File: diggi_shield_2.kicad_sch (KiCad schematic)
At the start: 100 parts, among them J1_P1 IN_L, J1_P2 IN_GND, J1_P3 IN_R, J1_P4 OUT_R, J1_P5 OUT_GND, J1_P6 OUT_L, J2_P1 HP_R, J2_P2 HP_GND, J2_P3 HP_L, J8_P1 GND, J8_P2 +5V, J8_P3 MIDI_RX*, J8_P4 MIDI_TX, J8_P5 VBUS_END

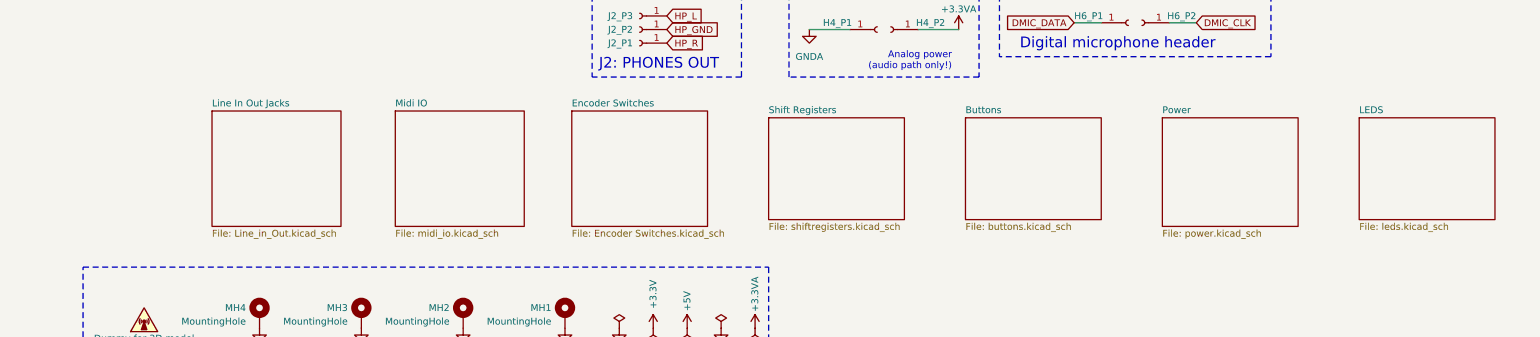
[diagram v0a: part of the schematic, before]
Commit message: Added oled hierarchical page and referenced other pages
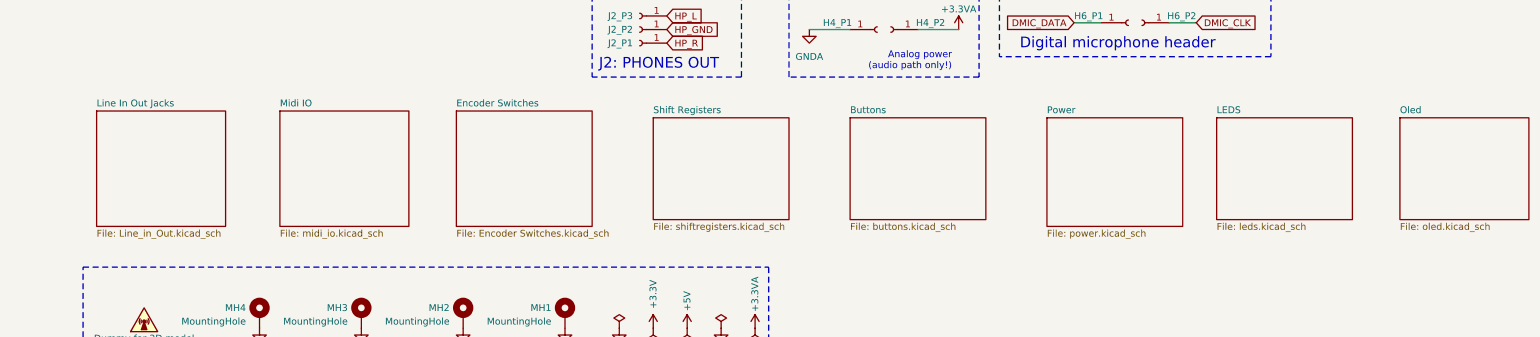
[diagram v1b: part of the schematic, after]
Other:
- added sheet Oled (oled.kicad_sch)
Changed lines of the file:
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@@
 			"AAAAAAAAAAAAAAAAAAAAAAAAAAAAAAAAAAAAAAAAAAAAAAAAAAAAAAAAAAAAAAAAAAAAAAAAAAAA"
 			"AAAAAAAAAAAAAAAAAAAAAAAAAAAAAAAAAAAAAAAAAAAAAAAAAAAAAAAAAAAAAAAAAAAAAAAAAAAA"
+			"AAAAAAAAAAAAAAAAAAAAAAAAAAAAAAAAAAAAAAAAAAAAAAAAAAAAAAAAAAAAAAAAAAAAAAAAAAAA"
+			"AAAAAAAAAAAAAAAAAAAAAAAAAAAAAAAAAAAAAAAAAAAAAAAAAAAAAAAAAAAAAAAAAAAAAAAAAAAA"
+			"AAAAAAAAAAAAAAAAAAAAAAAAAAAAAAAAAAAAAAAAAAAAAAAAAAAAAAAAAAAAAAAAAAAAAAAAAAAA"
+			"AAAAAAAAAAAAAAAAAAAAAAAAAAAAAAAAAAAAAAAAAAAAAAAAAAAAAAAAAAAAAAAAAAAAAAAAAAAA"
+			"AAAAAAAAAAAAAAAAAAAAAAAAAAAAAAAAAAAAAAAAAAAAAAAAAAAAAAAAAAAAAAAAAAAAAAAAAAAA"
+			"AAAAAAAAAAAAAAAAAAAAAAAAAAAAAAAAAAAAAAAAAAAAAAAAAAAAAAAAAAAAAAAAAAAAAAAAAAAA"
+			"AAAAAAAAAAAAAAAAAAAAAAAAAAAAAAAAAAAAAAAAAAAAAAAAAAAAAAAAAAAAAAAAAAAAAAAAAAAA"
+			"AAAAAAAAAAAAAAAAAAAAAAAAAAAAAAAAAAAAAAAAAAAAAAAAAAAAAAAAAAAAAAAAAAAAAAAAAAAA"
+			"AAAAAAAAAAAAAAAAAAAAAAAAAAAAAAAAAAAAAAAAAAAAAAAAAAAAAAAAAAAAAAAAAAAAAAAAAAAA"
+			"AAAAAAAAAAAAAAAAAAAAAAAAAAAAAAAAAAAAAAAAAAAAAAAAAAAAAAAAAAAAAAAAAAAAAAAAAAAA"
+			"AAAAAAAAAAAAAAAAAAAAAAAAAAAAAAAAAAAAAAAAAAAAAAAAAAAAAAAAAAAAAAAAAAAAAAAAAAAA"
+			"AAAAAAAAAAAAAAAAAAAAAAAAAAAAAAAAAAAAAAAAAAAAAAAAAAAAAAAAAAAAAAAAAAAAAAAAAAAA"
+			"AAAAAAAAAAAAAAAAAAAAAAAAAAAAAAAAAAAAAAAAAAAAAAAAAAAAAAAAAAAAAAAAAAAAAAAAAAAA"
+			"AAAAAAAAAAAAAAAAAAAAAAAAAAAAAAAAAAAAAAAAAAAAAAAAAAAAAAAAAAAAAAAAAAAAAAAAAAAA"
+			"AAAAAAAAAAAAAAAAAAAAAAAAAAAAAAAAAAAAAAAAAAAAAAAAAAAAAAAAAAAAAAAAAAAAAAAAAAAA"
+			"AAAAAAAAAAAAAAAAAAAAAAAAAAAAAAAAAAAAAAAAAAAAAAAAAAAAAAAAAAAAAAAAAAAAAAAAAAAA"
+			"AAAAAAAAAAAAAAAAAAAAAAAAAAAAAAAAAAAAAAAAAAAAAAAAAAAAAAAAAAAAAAAAAAAAAAAAAAAA"
+			"AAAAAAAAAAAAAAAAAAAAAAAAAAAAAAAAAAAAAAAAAAAAAAAAAAAAAAAAAAAAAAAAAAAAAAAAAAAA"
 			"AAAAAAAAAAAAAAAAAA=="
 		)
@@
 			"9X8BAPZ/AQD3fwEA+H8BAPl/AQD6fwEA+38BAPx/AQD9fwEA/n8BAP9/AQAAgAEAAYABAAKAAQAD"
 			"gAEABIABAAWAAQAGgAEAB4ABAAiAAQAJgAEACoABAAuAAQAMgAEADYABAA6AAQAPgAEAEIABABGA"
+			"ARYBAAAAkP6PFgEAAACQ/o8WAQAAAPBOcQcBAAAAkP6PFgEAAABQTXQHAQAAAADJkhYBAAAA0MiS"
+			"FgEAAADwSpEWAQAAAKDIkhYBAAAA8EqRFgEAAADwSpEWAQAAAHDIkhYBAAAAQMiSFgEAAADwWowW"
+			"AQAAAKBbgRYBAAAA8FqMFgEAAABQTXQHAQAAAFBNdAcBAAAAcDiSFgEAAACQ/o8WAQAAALBagRYB"
+			"AAAAkP6PFgEAAACwWoEWAQAAABDIkhYBAAAAsJmOFgEAAAAQW4EWAQAAALCZjhYBAAAAsJmOFgEA"
+			"AADgx5IWAQAAAPA2khYBAAAAsFqBFgEAAADwNpIWAQAAALDHkhYBAAAA8EqRFgEAAABwW4EWAQAA"
+			"APBKkRYBAAAA8EqRFgEAAADwSpEWAQAAAHBbgRYBAAAA8DaSFgEAAABwW4EWAQAAALCZjhYBAAAA"
+			"8DaSFgEAAABQTXQHAQAAAJD+jxYBAAAAkP6PFgEAAACQ/o8WAQAAAJD+jxYBAAAAkP6PFgEAAABQ"
+			"TXQHAQAAAIDHkhYBAAAAUMeSFgEAAADwSpEWAQAAACDHkhYBAAAA8EqRFgEAAADwSpEWAQAAAPDG"
+			"khYBAAAAoFuBFgEAAACwOJIWAQAAAFBNdAcBAAAAUE10BwEAAADAxpIWAQAAAHDRhhYBAAAAAN+A"
+			"FgEAAABw0YYWAQAAAHDRhhYBAAAAkMaSFgEAAABweegKAQAAAEDegBYBAAAAYMaSFgEAAABwougK"
+			"AQAAALBagRYBAAAAcFuBFgEAAAAwXIIWAQAAAHB56AoBAAAAcHnoCgEAAABweegKAQAAAHCi6AoB"
+			"AAAAcHnoCgEAAADAlugKAQAAADBpbgcBAAAAUE10BwEAAAAwaW4HAQAAADDGkhYBAAAAsEZyBwEA"
+			"AAAA34AWAQAAALBGcgcBAAAAsEZyBwEAAABgU4EWAQAAAMBTgRYBAAAAUE10BwEAAAAAxpIWAQAA"
+			"APA4khYBAAAAAN+AFgEAAADwOJIWAQAAAPA4khYBAAAA0MWSFgEAAACwRnIHAQAAAEDegBYBAAAA"
+			"oMWSFgEAAACwd24HAQAAAFBNdAcBAAAAsEZyBwEAAACwd24HAQAAALBGcgcBAAAAsHduBwEAAACw"
+			"RnIHAQAAAHDFkhYBAAAAQMWSFgEAAABweegKAQAAAEDegBYBAAAAcHnoCgEAAAAQxZIWAQAAALAV"
+			"cwcBAAAA4MSSFgEAAABweegKAQAAALDEkhYBAAAAoFuBFgEAAACwOJIWAQAAAFBNdAcBAAAAUE10"
+			"BwEAAACAxJIWAQAAAFDEkhYBAAAAsA6HFgEAAABQTXQHAQAAALAOhxYBAAAAIMSSFgEAAACwDocW"
 			"AQ=="
 		)
@@
 	)
 	(sheet
-		(at 36.83 147.32)
+		(at 15.24 147.32)
 		(size 24.13 21.59)
 		(exclude_from_sim no)
@@
 		)
 		(property "Sheetname" "Line In Out Jacks"
-			(at 36.83 146.6084 0)
+			(at 15.24 146.6084 0)
 			(effects
 				(font
@@
 		)
 		(property "Sheetfile" "Line_in_Out.kicad_sch"
-			(at 36.83 169.4946 0)
+			(at 15.24 169.4946 0)
 			(effects
 				(font
@@
 	)
 	(sheet
-		(at 71.12 147.32)
+		(at 49.53 147.32)
 		(size 24.13 21.59)
 		(exclude_from_sim no)
@@
 		)
 		(property "Sheetname" "Midi IO"
-			(at 71.12 146.6084 0)
+			(at 49.53 146.6084 0)
 			(effects
 				(font
@@
 		)
 		(property "Sheetfile" "midi_io.kicad_sch"
-			(at 71.12 169.4946 0)
+			(at 49.53 169.4946 0)
 			(effects
 				(font
@@
 	)
 	(sheet
-		(at 140.97 148.59)
+		(at 119.38 148.59)
 		(size 25.4 19.05)
 		(exclude_from_sim no)
@@
 		)
 		(fill
-			(color 0 0 0 0.0000)
+			(color 196 107 255 1.0000)
 		)
 		(property "Sheetname" "Shift Registers"
-			(at 140.97 147.8784 0)
+			(at 119.38 147.8784 0)
 			(effects
 				(font
@@
 		)
 		(property "Sheetfile" "shiftregisters.kicad_sch"
-			(at 140.97 168.2246 0)
+			(at 119.38 168.2246 0)
 			(effects
 				(font
@@
 	)
 	(sheet
-		(at 214.63 148.59)
+		(at 193.04 148.59)
 		(size 25.4 20.32)
 		(exclude_from_sim no)
@@
 		)
 		(property "Sheetname" "Power"
-			(at 214.63 147.8784 0)
+			(at 193.04 147.8784 0)
 			(effects
 				(font
@@
 		)
 		(property "Sheetfile" "power.kicad_sch"
-			(at 214.63 169.4946 0)
+			(at 193.04 169.4946 0)
 			(effects
 				(font
@@
 	)
 	(sheet
-		(at 104.14 147.32)
+		(at 82.55 147.32)
 		(size 25.4 21.59)
 		(exclude_from_sim no)
@@
 		)
 		(property "Sheetname" "Encoder Switches"
-			(at 104.14 146.6084 0)
+			(at 82.55 146.6084 0)
 			(effects
 				(font
@@
 		)
 		(property "Sheetfile" "Encoder Switches.kicad_sch"
-			(at 104.14 169.4946 0)
+			(at 82.55 169.4946 0)
 			(effects
 				(font
@@
 	)
 	(sheet
-		(at 251.46 148.59)
+		(at 224.79 148.59)
 		(size 25.4 19.05)
 		(exclude_from_sim no)
@@
 		)
 		(property "Sheetname" "LEDS"
-			(at 251.46 147.8784 0)
+			(at 224.79 147.8784 0)
 			(effects
 				(font
@@
 		)
 		(property "Sheetfile" "leds.kicad_sch"
-			(at 251.46 168.2246 0)
+			(at 224.79 168.2246 0)
 			(effects
 				(font
@@
 	)
 	(sheet
-		(at 177.8 148.59)
+		(at 156.21 148.59)
 		(size 25.4 19.05)
 		(exclude_from_sim no)
@@
 		)
 		(fill
-			(color 0 0 0 0.0000)
+			(color 80 255 184 1.0000)
 		)
 		(property "Sheetname" "Buttons"
-			(at 177.8 147.8784 0)
+			(at 156.21 147.8784 0)
 			(effects
 				(font
@@
 		)
 		(property "Sheetfile" "buttons.kicad_sch"
-			(at 177.8 168.2246 0)
+			(at 156.21 168.2246 0)
 			(effects
 				(font
@@
 				)
 			)
+		)
+	)
+	(sheet
+		(at 259.08 148.59)
+		(size 24.13 19.05)
+		(exclude_from_sim no)
+		(in_bom yes)
+		(on_board yes)
+		(dnp no)
+		(fields_autoplaced yes)
+		(stroke
+			(width 0.1524)
+			(type solid)
+		)
+		(fill
+			(color 255 126 20 1.0000)
+		)
+		(property "Sheetname" "Oled"
+			(at 259.08 147.8784 0)
+			(effects
+				(font
+					(size 1.27 1.27)
+				)
+				(justify left bottom)
+			)
+		)
+		(property "Sheetfile" "oled.kicad_sch"
+			(at 259.08 168.2246 0)
+			(effects
+				(font
+					(size 1.27 1.27)
+				)
+				(justify left top)
+			)
+		)
+		(instances
+			(project "diggi_shield_2"
+				(path "/21684161-6457-4723-8fc3-25d7330779e2"
+					(page "9")
+				)
+			)

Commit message: Female to socket symbol
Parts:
- H1_P1, H1_P10, H1_P11, H1_P12, H1_P13, H1_P14, H1_P15, H1_P16, H1_P17, H1_P18, H1_P19, H1_P2, H1_P20, H1_P21, H1_P22, H1_P23, H1_P24, H1_P3, H1_P4, H1_P5, H1_P6, H1_P7, H1_P8, H1_P9, H2_P1, H2_P10, H2_P11, H2_P12, H2_P13, H2_P14, H2_P15, H2_P16, H2_P17, H2_P18, H2_P19, H2_P2, H2_P20, H2_P21, H2_P22, H2_P23, H2_P24, H2_P3, H2_P4, H2_P5, H2_P6, H2_P7, H2_P8, H2_P9, H3_P1, H3_P10, H3_P11, H3_P12, H3_P13, H3_P14, H3_P15, H3_P16, H3_P17, H3_P18, H3_P19, H3_P2, H3_P20, H3_P21, H3_P22, H3_P23, H3_P24, H3_P25, H3_P26, H3_P3, H3_P4, H3_P5, H3_P6, H3_P7, H3_P8, H3_P9, H4_P1, H4_P2, H5_P1, H5_P2, H5_P3, H6_P1, H6_P2, J1_P1, J1_P2, J1_P3, J1_P4, J1_P5, J1_P6, J2_P1, J2_P2, J2_P3, J8_P1, J8_P2, J8_P3, J8_P4, J8_P5: symbol Connector:Conn_01x01_Female -> Connector:Conn_01x01_Socket

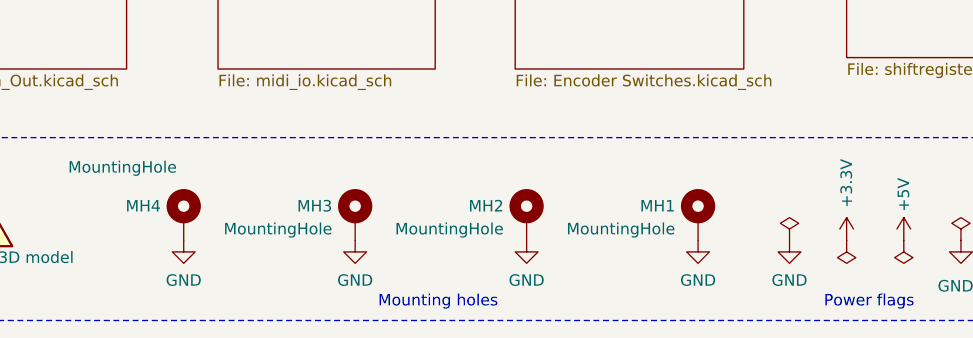
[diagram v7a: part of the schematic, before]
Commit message: Remove symbol copy warnings
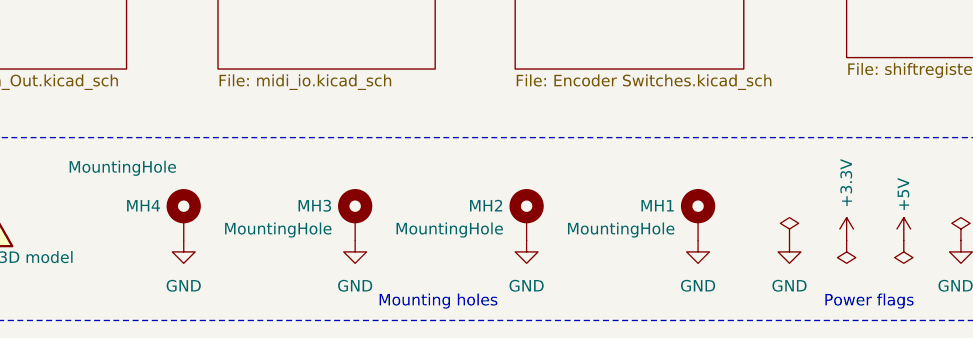
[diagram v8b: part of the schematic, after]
